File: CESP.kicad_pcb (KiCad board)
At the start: 2 copper layers, 55.9 x 44.7 mm, 9 parts

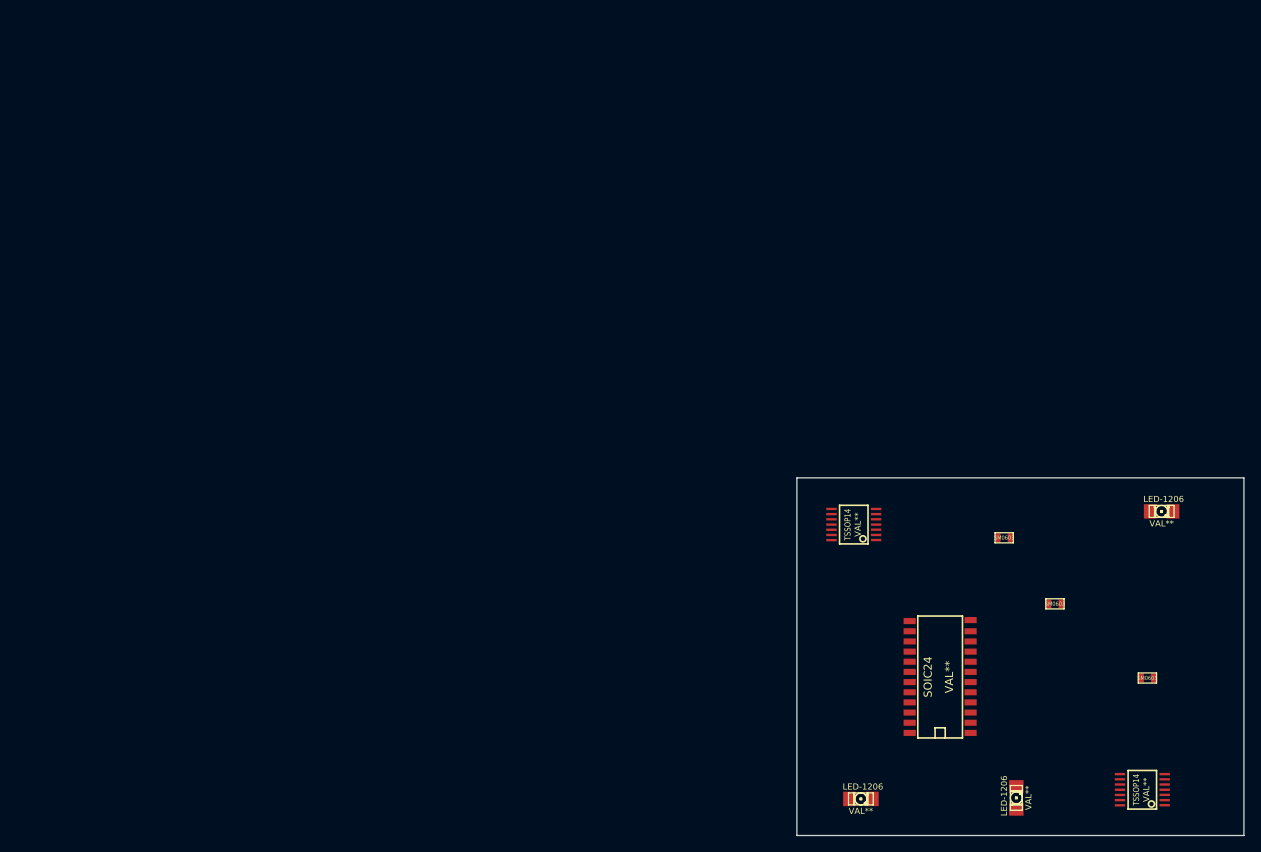
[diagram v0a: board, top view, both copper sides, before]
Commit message: new solder board
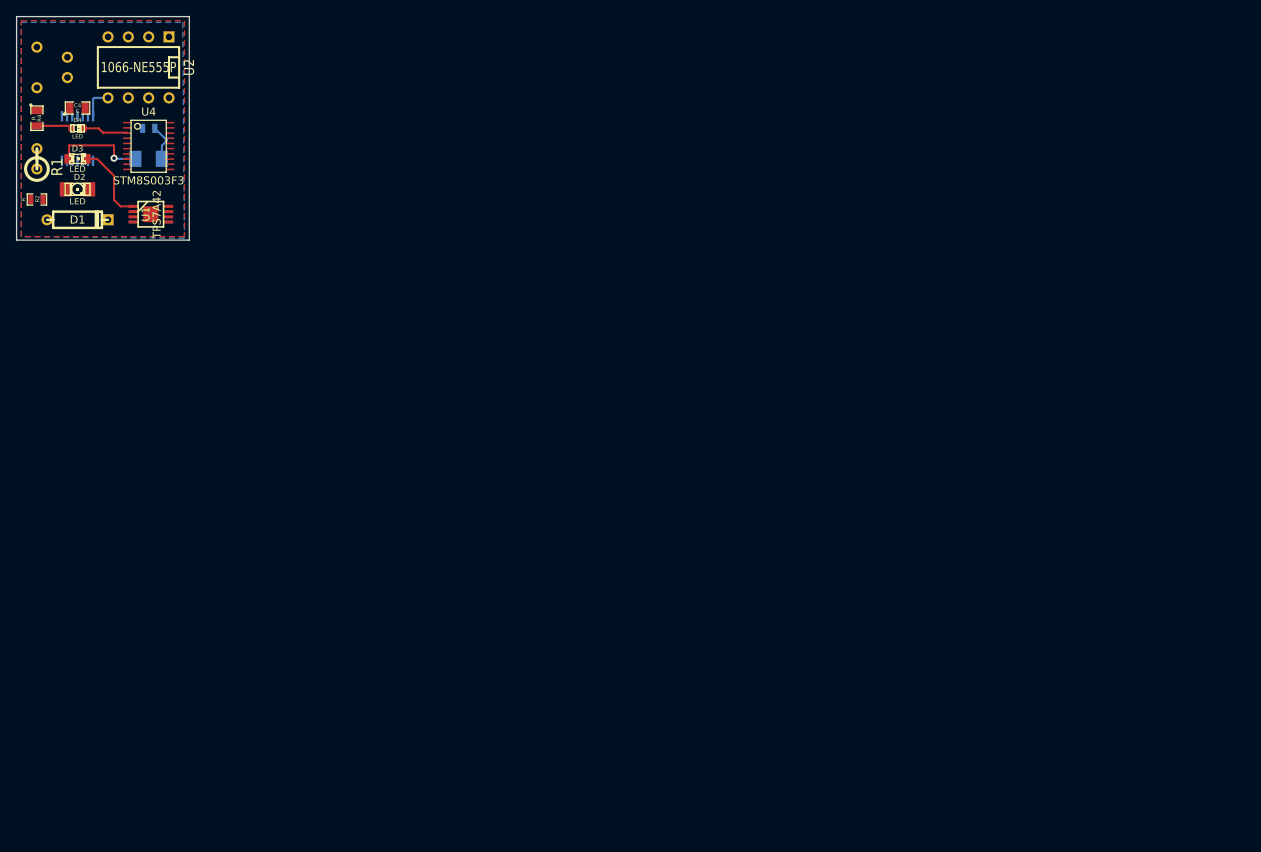
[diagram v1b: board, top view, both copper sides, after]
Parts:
- removed LED-1206 (x3): VAL**, LED-1206
- removed SM0603 (x3): Val**, SM0603
- removed SOIC24: VAL**, SOIC24
- removed TSSOP14 (x2): VAL**, TSSOP14
- added C1: C, C1, B.Cu at (64.8, 44.5)
- added C2: C, C2, B.Cu at (61.0, 44.5)
- added C3: C, SM0603_Capa, B.Cu at (74.9, 52.1)
- added C4: C, SM0805, F.Cu at (66.0, 49.5)
- added D1: LED, D3, F.Cu at (66.0, 63.5)
- added D2: LED, LED-1206, F.Cu at (66.0, 59.7)
- added D3: LED, LED-0805, F.Cu at (66.0, 55.9)
- added D4: LED, LED-0603, F.Cu at (66.0, 52.1)
- added R1: R, R1, F.Cu at (61.0, 55.9)
- added R2: R, SM0603_Resistor, F.Cu at (61.0, 61.0)
- added R3: R, SM1206, B.Cu at (74.9, 55.9)
- added R4: R, SM0805, F.Cu at (61.0, 50.8)
- added U1: TPS7A42, MSOP_8_PowerPad, F.Cu at (75.2, 62.8)
- added U2: 1066-NE555P, DIP-8__300, F.Cu at (73.7, 44.5)
- added U3: 4066, TSSOP14, B.Cu at (66.0, 53.3)
- added U4: STM8S003F3, tssop20, F.Cu at (74.9, 54.6)
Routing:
- net N-0000010: track 0.00 -> 11.6 mm, vias 0 -> 1
- net N-0000020: track 0.00 -> 10.2 mm
- net N-0000018: track 0.00 -> 5.69 mm
- net N-0000011: track 0.00 -> 4.69 mm
- net N-000008: track 0.00 -> 4.46 mm
- net N-0000019: track 0.00 -> 4.06 mm
- added copper zone on B.Cu, net (none)
- added copper zone on F.Cu, net (none)
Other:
- board size 55.9 x 44.7 mm -> 21.6 x 27.9 mm
- board text removed: "NOTE: THIS IS JUST A TEST BOARD REMOVE ALL COMPONENTS AND CREATE YOUR OWN INCLUDE SCHEMATIC HOOKUPS/NETLIST"
